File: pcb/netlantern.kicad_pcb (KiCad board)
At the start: 2 copper layers, 45 x 90 mm, 60 parts

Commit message: working on stuff
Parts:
- added REF**: ESP-32S, ESP32-footprints-Lib:ESP-32S, B.Cu at (117.5, 156.5)
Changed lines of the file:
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@@
     (tracks 0)
     (zones 0)
-    (modules 60)
+    (modules 61)
     (nets 1)
   )
@@
     )
   )
+  (module ESP32-footprints-Lib:ESP-32S (layer B.Cu)
+    (at 117.5 156.5)
+    (fp_text reference REF** (at -9.9 13.8 -270) (layer B.SilkS)
+      (effects (font (size 1 1) (thickness 0.15)) (justify mirror))
+    )
+    (fp_text value ESP-32S (at 0.7 12.3) (layer B.Fab)
+      (effects (font (size 1 1) (thickness 0.15)) (justify mirror))
+    )
+    (fp_line (start 8.947434 17.017338) (end -9.052566 17.017338) (layer B.SilkS) (width 0.15))
+    (fp_line (start 8.947434 -8.482662) (end -9.052566 -8.482662) (layer B.SilkS) (width 0.15))
+    (fp_line (start 8.947434 17.017338) (end 8.947434 -8.482662) (layer B.SilkS) (width 0.15))
+    (fp_line (start -9.052566 17.017338) (end -9.052566 -8.482662) (layer B.SilkS) (width 0.15))
+    (fp_line (start 8.947434 11.017338) (end -9.052566 11.017338) (layer B.SilkS) (width 0.15))
+    (fp_text user ESP-32S (at 4.8 -2.8 -90) (layer B.SilkS)
+      (effects (font (size 1 1) (thickness 0.15)) (justify mirror))
+    )
+    (fp_circle (center -9.958566 10.871338) (end -10.085566 11.125338) (layer B.SilkS) (width 0.5))
+    (fp_text user AI-Thinker/Espressif (at 6.3 1.6 -90) (layer B.SilkS)
+      (effects (font (size 1 1) (thickness 0.15)) (justify mirror))
+    )
+    (pad 39 smd rect (at -0.352566 1.817338 180) (size 6 6) (layers B.Cu B.Paste B.Mask))
+    (pad 1 smd oval (at -9.052566 9.517338 180) (size 2.5 0.9) (layers B.Cu B.Paste B.Mask))
+    (pad 2 smd oval (at -9.052566 8.247338 180) (size 2.5 0.9) (layers B.Cu B.Paste B.Mask))
+    (pad 3 smd oval (at -9.052566 6.977338 180) (size 2.5 0.9) (layers B.Cu B.Paste B.Mask))
+    (pad 4 smd oval (at -9.052566 5.707338 180) (size 2.5 0.9) (layers B.Cu B.Paste B.Mask))
+    (pad 5 smd oval (at -9.052566 4.437338 180) (size 2.5 0.9) (layers B.Cu B.Paste B.Mask))
+    (pad 6 smd oval (at -9.052566 3.167338 180) (size 2.5 0.9) (layers B.Cu B.Paste B.Mask))
+    (pad 7 smd oval (at -9.052566 1.897338 180) (size 2.5 0.9) (layers B.Cu B.Paste B.Mask))
+    (pad 8 smd oval (at -9.052566 0.627338 180) (size 2.5 0.9) (layers B.Cu B.Paste B.Mask))
+    (pad 9 smd oval (at -9.052566 -0.642662 180) (size 2.5 0.9) (layers B.Cu B.Paste B.Mask))
+    (pad 10 smd oval (at -9.052566 -1.912662 180) (size 2.5 0.9) (layers B.Cu B.Paste B.Mask))
+    (pad 11 smd oval (at -9.052566 -3.182662 180) (size 2.5 0.9) (layers B.Cu B.Paste B.Mask))
+    (pad 12 smd oval (at -9.052566 -4.452662 180) (size 2.5 0.9) (layers B.Cu B.Paste B.Mask))
+    (pad 13 smd oval (at -9.052566 -5.722662 180) (size 2.5 0.9) (layers B.Cu B.Paste B.Mask))
+    (pad 14 smd oval (at -9.052566 -6.992662 180) (size 2.5 0.9) (layers B.Cu B.Paste B.Mask))
+    (pad 15 smd oval (at -5.767566 -8.482662 180) (size 0.9 2.5) (layers B.Cu B.Paste B.Mask))
+    (pad 16 smd oval (at -4.497566 -8.482662 180) (size 0.9 2.5) (layers B.Cu B.Paste B.Mask))
+    (pad 17 smd oval (at -3.227566 -8.482662 180) (size 0.9 2.5) (layers B.Cu B.Paste B.Mask))
+    (pad 18 smd oval (at -1.957566 -8.482662 180) (size 0.9 2.5) (layers B.Cu B.Paste B.Mask))
+    (pad 19 smd oval (at -0.687566 -8.482662 180) (size 0.9 2.5) (layers B.Cu B.Paste B.Mask))
+    (pad 20 smd oval (at 0.582434 -8.482662 180) (size 0.9 2.5) (layers B.Cu B.Paste B.Mask))
+    (pad 21 smd oval (at 1.852434 -8.482662 180) (size 0.9 2.5) (layers B.Cu B.Paste B.Mask))
+    (pad 22 smd oval (at 3.122434 -8.482662 180) (size 0.9 2.5) (layers B.Cu B.Paste B.Mask))
+    (pad 23 smd oval (at 4.392434 -8.482662 180) (size 0.9 2.5) (layers B.Cu B.Paste B.Mask))
+    (pad 24 smd oval (at 5.662434 -8.482662 180) (size 0.9 2.5) (layers B.Cu B.Paste B.Mask))
+    (pad 25 smd oval (at 8.947434 -6.992662 180) (size 2.5 0.9) (layers B.Cu B.Paste B.Mask))
+    (pad 26 smd oval (at 8.947434 -5.722662 180) (size 2.5 0.9) (layers B.Cu B.Paste B.Mask))
+    (pad 27 smd oval (at 8.947434 -4.452662 180) (size 2.5 0.9) (layers B.Cu B.Paste B.Mask))
+    (pad 28 smd oval (at 8.947434 -3.182662 180) (size 2.5 0.9) (layers B.Cu B.Paste B.Mask))
+    (pad 29 smd oval (at 8.947434 -1.912662 180) (size 2.5 0.9) (layers B.Cu B.Paste B.Mask))
+    (pad 30 smd oval (at 8.947434 -0.642662 180) (size 2.5 0.9) (layers B.Cu B.Paste B.Mask))
+    (pad 31 smd oval (at 8.947434 0.627338 180) (size 2.5 0.9) (layers B.Cu B.Paste B.Mask))
+    (pad 32 smd oval (at 8.947434 1.897338 180) (size 2.5 0.9) (layers B.Cu B.Paste B.Mask))
+    (pad 33 smd oval (at 8.947434 3.167338 180) (size 2.5 0.9) (layers B.Cu B.Paste B.Mask))
+    (pad 34 smd oval (at 8.947434 4.437338 180) (size 2.5 0.9) (layers B.Cu B.Paste B.Mask))
+    (pad 35 smd oval (at 8.947434 5.707338 180) (size 2.5 0.9) (layers B.Cu B.Paste B.Mask))
+    (pad 36 smd oval (at 8.947434 6.977338 180) (size 2.5 0.9) (layers B.Cu B.Paste B.Mask))
+    (pad 37 smd oval (at 8.947434 8.247338 180) (size 2.5 0.9) (layers B.Cu B.Paste B.Mask))
+    (pad 38 smd oval (at 8.947434 9.517338 180) (size 2.5 0.9) (layers B.Cu B.Paste B.Mask))
+  )
   (gr_line (start 140 90) (end 140 180) (layer Edge.Cuts) (width 0.15))

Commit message: decided to do in parts - led board ready to send
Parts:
- removed REF** (x2): Pin_d1.3mm_L11.3mm_W2.8mm_Flat, Connectors:Pin_d1.3mm_L11.3mm_W2.8mm_Flat
- removed REF** (x24): C_0805_HandSoldering, Capacitors_SMD:C_0805_HandSoldering
- removed REF** (x2): Pin_Header_Straight_1x08_Pitch2.54mm, Pin_Headers:Pin_Header_Straight_1x08_Pitch2.54mm
- removed REF**: ESP-32S, ESP32-footprints-Lib:ESP-32S
- added C1: 100n, Capacitor_SMD:C_0805_2012Metric_Pad1.15x1.40mm_HandSolder, F.Cu at (107.5, 100.0)
- added C10: 100n, Capacitor_SMD:C_0805_2012Metric_Pad1.15x1.40mm_HandSolder, F.Cu at (107.5, 130.0)
- added C11: 100n, Capacitor_SMD:C_0805_2012Metric_Pad1.15x1.40mm_HandSolder, F.Cu at (117.5, 130.0)
- added C12: 100n, Capacitor_SMD:C_0805_2012Metric_Pad1.15x1.40mm_HandSolder, F.Cu at (127.5, 130.0)
- added C13: 100n, Capacitor_SMD:C_0805_2012Metric_Pad1.15x1.40mm_HandSolder, F.Cu at (107.5, 140.0)
- added C14: 100n, Capacitor_SMD:C_0805_2012Metric_Pad1.15x1.40mm_HandSolder, F.Cu at (117.5, 140.0)
- added C15: 100n, Capacitor_SMD:C_0805_2012Metric_Pad1.15x1.40mm_HandSolder, F.Cu at (127.5, 140.0)
- added C16: 100n, Capacitor_SMD:C_0805_2012Metric_Pad1.15x1.40mm_HandSolder, F.Cu at (107.5, 150.0)
- added C17: 100n, Capacitor_SMD:C_0805_2012Metric_Pad1.15x1.40mm_HandSolder, F.Cu at (117.5, 150.0)
- added C18: 100n, Capacitor_SMD:C_0805_2012Metric_Pad1.15x1.40mm_HandSolder, F.Cu at (127.5, 150.0)
- added C19: 100n, Capacitor_SMD:C_0805_2012Metric_Pad1.15x1.40mm_HandSolder, F.Cu at (107.5, 160.0)
- added C2: 100n, Capacitor_SMD:C_0805_2012Metric_Pad1.15x1.40mm_HandSolder, F.Cu at (117.5, 100.0)
- added C20: 100n, Capacitor_SMD:C_0805_2012Metric_Pad1.15x1.40mm_HandSolder, F.Cu at (117.5, 160.0)
- added C21: 100n, Capacitor_SMD:C_0805_2012Metric_Pad1.15x1.40mm_HandSolder, F.Cu at (127.5, 160.0)
- added C22: 100n, Capacitor_SMD:C_0805_2012Metric_Pad1.15x1.40mm_HandSolder, F.Cu at (107.5, 170.0)
- added C23: 100n, Capacitor_SMD:C_0805_2012Metric_Pad1.15x1.40mm_HandSolder, F.Cu at (117.5, 170.0)
- added C24: 100n, Capacitor_SMD:C_0805_2012Metric_Pad1.15x1.40mm_HandSolder, F.Cu at (127.5, 170.0)
- added C25: 10u, Capacitor_SMD:C_1206_3216Metric_Pad1.42x1.75mm_HandSolder, B.Cu at (117.5, 93.0)
- added C26: 10u, Capacitor_SMD:C_1206_3216Metric_Pad1.42x1.75mm_HandSolder, B.Cu at (117.5, 172.5)
- added C3: 100n, Capacitor_SMD:C_0805_2012Metric_Pad1.15x1.40mm_HandSolder, F.Cu at (127.5, 100.0)
- added C4: 100n, Capacitor_SMD:C_0805_2012Metric_Pad1.15x1.40mm_HandSolder, F.Cu at (107.5, 110.0)
- added C5: 100n, Capacitor_SMD:C_0805_2012Metric_Pad1.15x1.40mm_HandSolder, F.Cu at (117.5, 110.0)
- added C6: 100n, Capacitor_SMD:C_0805_2012Metric_Pad1.15x1.40mm_HandSolder, F.Cu at (127.5, 110.0)
- added C7: 100n, Capacitor_SMD:C_0805_2012Metric_Pad1.15x1.40mm_HandSolder, F.Cu at (107.5, 120.0)
- added C8: 100n, Capacitor_SMD:C_0805_2012Metric_Pad1.15x1.40mm_HandSolder, F.Cu at (117.5, 120.0)
- added C9: 100n, Capacitor_SMD:C_0805_2012Metric_Pad1.15x1.40mm_HandSolder, F.Cu at (127.5, 120.0)
- added J1: Screw_Terminal_01x04, Morn_Mechanical:TerminalBlock_Phoenix_PTSM-0,5-4-2,5-V-SMD_1x04_P2.50mm_Horizontal, B.Cu at (117.5, 161.0)
- D1, D10, D11, D12, D13, D14, D15, D16, D17, D18, D19, D2, D20, D21, D22, D23, D24, D25, D26, D27, D28, D29, D3, D30, D31, D32, D4, D5, D6, D7, D8, D9: renamed from REF**; value LED_WS2812B-PLCC4 -> WS2812B
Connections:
- D1 pad 1: (no net) -> +5V
- D1 pad 2: (no net) -> Net-(D1-Pad2)
- D1 pad 3: (no net) -> GND
- D1 pad 4: (no net) -> /DIN
- D10 pad 1: (no net) -> +5V
- D10 pad 2: (no net) -> Net-(D10-Pad2)
- D10 pad 3: (no net) -> GND
- D10 pad 4: (no net) -> Net-(D10-Pad4)
- D11 pad 1: (no net) -> +5V
- D11 pad 2: (no net) -> Net-(D11-Pad2)
- D11 pad 3: (no net) -> GND
- D11 pad 4: (no net) -> Net-(D10-Pad2)
- D12 pad 1: (no net) -> +5V
- D12 pad 2: (no net) -> Net-(D12-Pad2)
- D12 pad 3: (no net) -> GND
- D12 pad 4: (no net) -> Net-(D11-Pad2)
- D13 pad 1: (no net) -> +5V
- D13 pad 2: (no net) -> Net-(D13-Pad2)
- D13 pad 3: (no net) -> GND
- D13 pad 4: (no net) -> Net-(D12-Pad2)
- D14 pad 1: (no net) -> +5V
- D14 pad 2: (no net) -> Net-(D14-Pad2)
- D14 pad 3: (no net) -> GND
- D14 pad 4: (no net) -> Net-(D13-Pad2)
- D15 pad 1: (no net) -> +5V
- D15 pad 2: (no net) -> Net-(D15-Pad2)
- D15 pad 3: (no net) -> GND
- D15 pad 4: (no net) -> Net-(D14-Pad2)
- D16 pad 1: (no net) -> +5V
- D16 pad 2: (no net) -> Net-(D16-Pad2)
- D16 pad 3: (no net) -> GND
- D16 pad 4: (no net) -> Net-(D15-Pad2)
- D17 pad 1: (no net) -> +5V
- D17 pad 2: (no net) -> Net-(D17-Pad2)
- D17 pad 3: (no net) -> GND
- D17 pad 4: (no net) -> Net-(D16-Pad2)
- D18 pad 1: (no net) -> +5V
- D18 pad 2: (no net) -> Net-(D18-Pad2)
- D18 pad 3: (no net) -> GND
- D18 pad 4: (no net) -> Net-(D17-Pad2)
- D19 pad 1: (no net) -> +5V
- D19 pad 2: (no net) -> Net-(D19-Pad2)
- D19 pad 3: (no net) -> GND
- D19 pad 4: (no net) -> Net-(D18-Pad2)
- D2 pad 1: (no net) -> +5V
- D2 pad 2: (no net) -> Net-(D2-Pad2)
- D2 pad 3: (no net) -> GND
- D2 pad 4: (no net) -> Net-(D1-Pad2)
- D20 pad 1: (no net) -> +5V
- D20 pad 2: (no net) -> Net-(D20-Pad2)
- D20 pad 3: (no net) -> GND
- D20 pad 4: (no net) -> Net-(D19-Pad2)
- D21 pad 1: (no net) -> +5V
- D21 pad 2: (no net) -> Net-(D21-Pad2)
- D21 pad 3: (no net) -> GND
- D21 pad 4: (no net) -> Net-(D20-Pad2)
- D22 pad 1: (no net) -> +5V
- D22 pad 2: (no net) -> Net-(D22-Pad2)
- D22 pad 3: (no net) -> GND
- D22 pad 4: (no net) -> Net-(D21-Pad2)
- D23 pad 1: (no net) -> +5V
- D23 pad 2: (no net) -> Net-(D23-Pad2)
- D23 pad 3: (no net) -> GND
- D23 pad 4: (no net) -> Net-(D22-Pad2)
- D24 pad 1: (no net) -> +5V
- D24 pad 2: (no net) -> Net-(D24-Pad2)
- D24 pad 3: (no net) -> GND
- D24 pad 4: (no net) -> Net-(D23-Pad2)
- D25 pad 1: (no net) -> +5V
- D25 pad 2: (no net) -> Net-(D25-Pad2)
- D25 pad 3: (no net) -> GND
- D25 pad 4: (no net) -> Net-(D24-Pad2)
- D26 pad 1: (no net) -> +5V
- D26 pad 2: (no net) -> Net-(D26-Pad2)
- D26 pad 3: (no net) -> GND
- D26 pad 4: (no net) -> Net-(D25-Pad2)
- D27 pad 1: (no net) -> +5V
- D27 pad 2: (no net) -> Net-(D27-Pad2)
- D27 pad 3: (no net) -> GND
- D27 pad 4: (no net) -> Net-(D26-Pad2)
- D28 pad 1: (no net) -> +5V
- D28 pad 2: (no net) -> Net-(D28-Pad2)
- D28 pad 3: (no net) -> GND
- D28 pad 4: (no net) -> Net-(D27-Pad2)
- D29 pad 1: (no net) -> +5V
- D29 pad 2: (no net) -> Net-(D29-Pad2)
- D29 pad 3: (no net) -> GND
- D29 pad 4: (no net) -> Net-(D28-Pad2)
- D3 pad 1: (no net) -> +5V
- D3 pad 2: (no net) -> Net-(D3-Pad2)
- D3 pad 3: (no net) -> GND
- D3 pad 4: (no net) -> Net-(D2-Pad2)
- D30 pad 1: (no net) -> +5V
- D30 pad 2: (no net) -> Net-(D30-Pad2)
- D30 pad 3: (no net) -> GND
- D30 pad 4: (no net) -> Net-(D29-Pad2)
- D31 pad 1: (no net) -> +5V
- D31 pad 2: (no net) -> Net-(D31-Pad2)
- D31 pad 3: (no net) -> GND
- D31 pad 4: (no net) -> Net-(D30-Pad2)
- D32 pad 1: (no net) -> +5V
- D32 pad 2: (no net) -> /DOUT
- D32 pad 3: (no net) -> GND
- D32 pad 4: (no net) -> Net-(D31-Pad2)
- D4 pad 1: (no net) -> +5V
- D4 pad 2: (no net) -> Net-(D4-Pad2)
- D4 pad 3: (no net) -> GND
- D4 pad 4: (no net) -> Net-(D3-Pad2)
- D5 pad 1: (no net) -> +5V
- D5 pad 2: (no net) -> Net-(D5-Pad2)
- D5 pad 3: (no net) -> GND
- D5 pad 4: (no net) -> Net-(D4-Pad2)
- D6 pad 1: (no net) -> +5V
- D6 pad 2: (no net) -> Net-(D6-Pad2)
- D6 pad 3: (no net) -> GND
- D6 pad 4: (no net) -> Net-(D5-Pad2)
- D7 pad 1: (no net) -> +5V
- D7 pad 2: (no net) -> Net-(D7-Pad2)
- D7 pad 3: (no net) -> GND
- D7 pad 4: (no net) -> Net-(D6-Pad2)
- D8 pad 1: (no net) -> +5V
- D8 pad 2: (no net) -> Net-(D8-Pad2)
- D8 pad 3: (no net) -> GND
- D8 pad 4: (no net) -> Net-(D7-Pad2)
- D9 pad 1: (no net) -> +5V
- D9 pad 2: (no net) -> Net-(D10-Pad4)
- D9 pad 3: (no net) -> GND
- D9 pad 4: (no net) -> Net-(D8-Pad2)
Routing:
- net GND: track 0.00 -> 454.4 mm, vias 0 -> 15
- net +5V: track 0.00 -> 82.4 mm, vias 0 -> 8
- net /DIN: track 0.00 -> 81.2 mm, vias 0 -> 1
- net Net-(D20-Pad2): track 0.00 -> 36.0 mm
- net Net-(D28-Pad2): track 0.00 -> 35.6 mm
- net Net-(D24-Pad2): track 0.00 -> 35.6 mm
- net Net-(D8-Pad2): track 0.00 -> 35.6 mm
- net Net-(D4-Pad2): track 0.00 -> 35.6 mm
- net Net-(D12-Pad2): track 0.00 -> 35.6 mm
- net Net-(D16-Pad2): track 0.00 -> 35.4 mm
- net /DOUT: track 0.00 -> 18.3 mm, vias 0 -> 1
- net Net-(D30-Pad2): track 0.00 -> 9.22 mm
- net Net-(D29-Pad2): track 0.00 -> 9.22 mm
- net Net-(D26-Pad2): track 0.00 -> 9.22 mm
- net Net-(D25-Pad2): track 0.00 -> 9.22 mm
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- added copper zone on F.Cu, net +5V
- added copper zone on B.Cu, net GND
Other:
- rule via_min_size: 0.4 -> 0.6
- board text added: "Tobias Kaiser / netlantern LED board / Sep 21 2018"

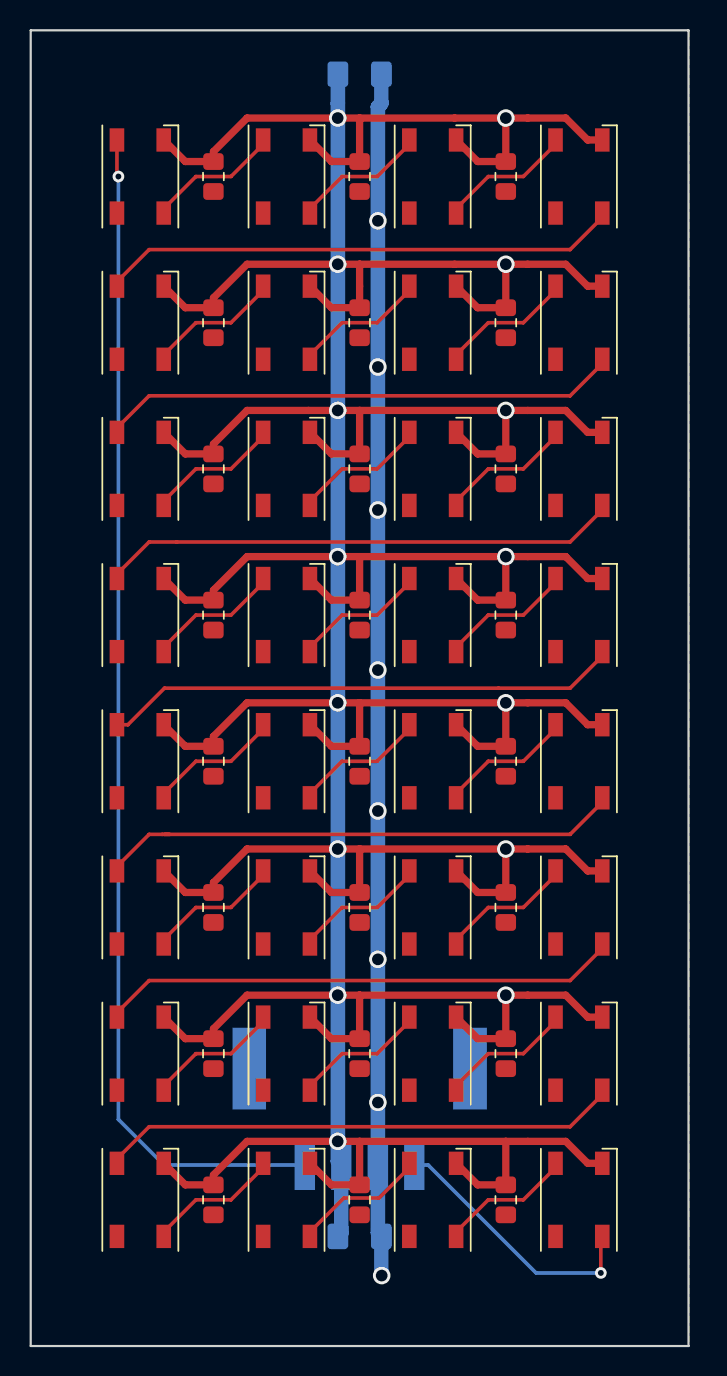
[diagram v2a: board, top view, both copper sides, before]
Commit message: added more connectors
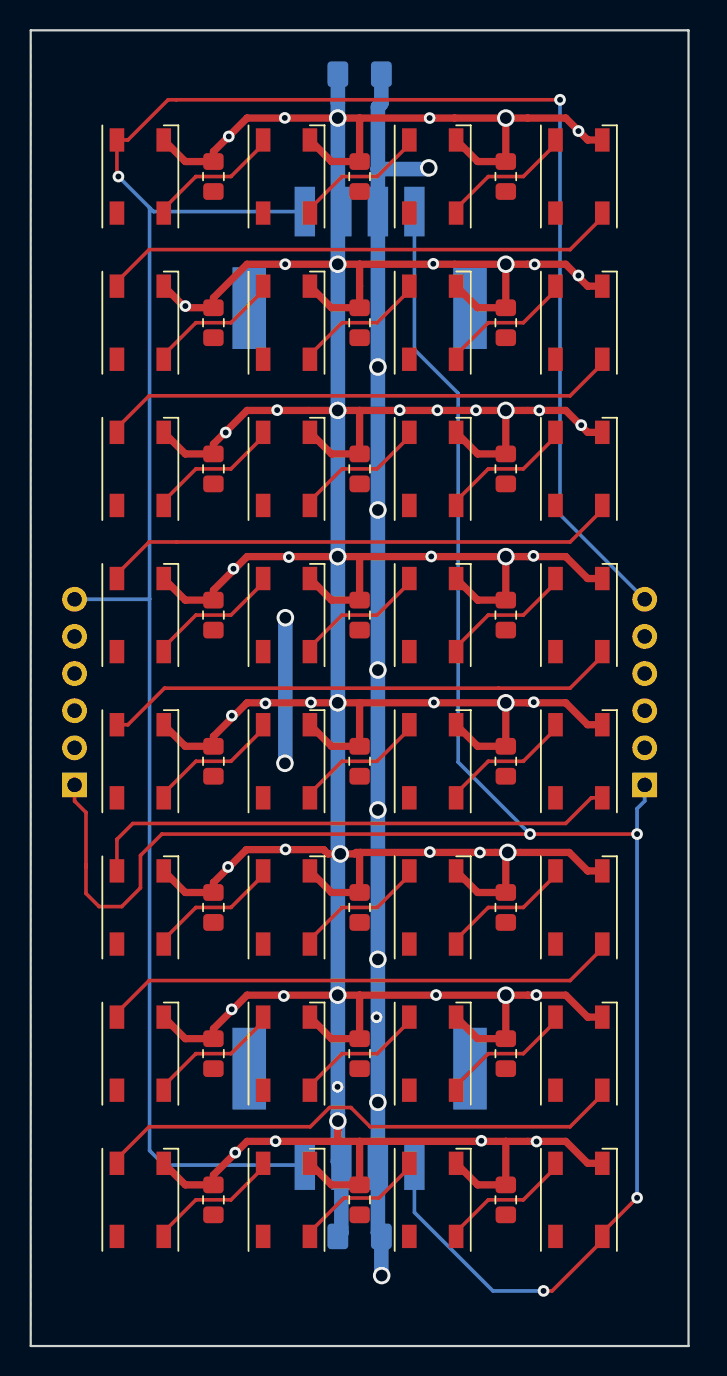
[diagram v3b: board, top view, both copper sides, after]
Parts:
- added J2: Conn_01x06, Connector_PinSocket_2.54mm:PinSocket_1x06_P2.54mm_Vertical, B.Cu at (98.0, 141.6)
- added J3: Conn_01x06, Connector_PinSocket_2.54mm:PinSocket_1x06_P2.54mm_Vertical, B.Cu at (137.0, 141.6)
- added J4: Screw_Terminal_01x04, Morn_Mechanical:TerminalBlock_Phoenix_PTSM-0,5-4-2,5-V-SMD_1x04_P2.50mm_Horizontal, B.Cu at (117.5, 109.0)
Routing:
- net /DOUT: track 18.3 -> 147.5 mm, vias 1 -> 4
- net /DIN: track 81.2 -> 165.1 mm, vias 1 -> 2
- net +5V: track 82.4 -> 95.9 mm, vias 8 -> 11
- net GND: track 454.4 -> 456.0 mm, vias 15 -> 53
- net Net-(D28-Pad2): track 35.6 -> 36.7 mm
- net Net-(D20-Pad2): track 36.0 -> 36.8 mm
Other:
- board text added: "DIN GND 5V DOUT"
- board text added: "DIN GND GND 5V 5V DOUT"
- board text added: "Tobias Kaiser netlantern LED board Sep 21 2018"
- board text removed: "Tobias Kaiser / netlantern LED board / Sep 21 2018"
